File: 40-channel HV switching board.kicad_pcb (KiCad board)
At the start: 2 copper layers, 83.8 x 121.9 mm, 211 parts, among them IC1 ATMEG328PU, J1 CONN_01X04, J2 CONN_01X10, J3 BNC, J4 BNC, J5 CONN_01X40, P1 CONN_01X06, P2 CONN_01X06, SW1 Switch_DPST, U1 74HC595A, U2 74HC595A, U3 74HC595A, U4 74HC595A, U5 74HC595A, U6 7400, X1 16MHz

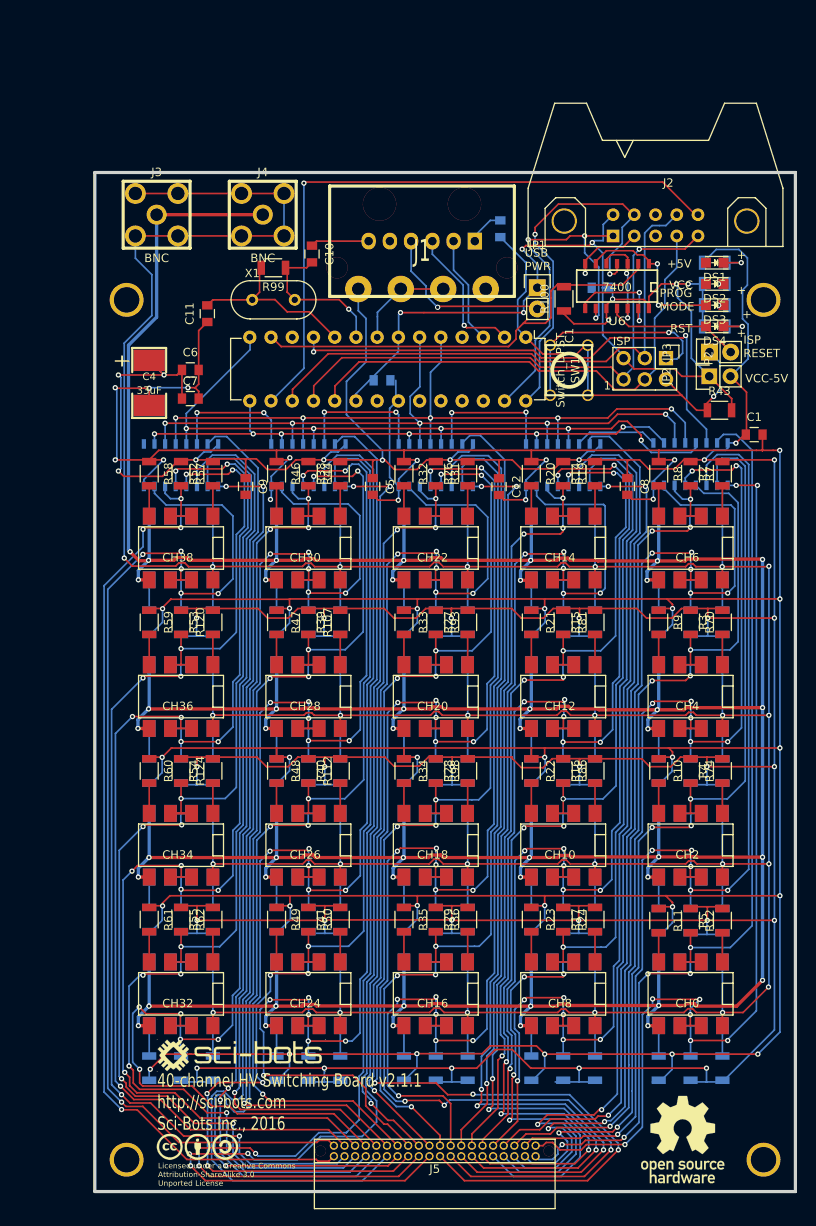
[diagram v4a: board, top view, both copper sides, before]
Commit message: Use edge connector, 3.3V logic, smaller board, etc.
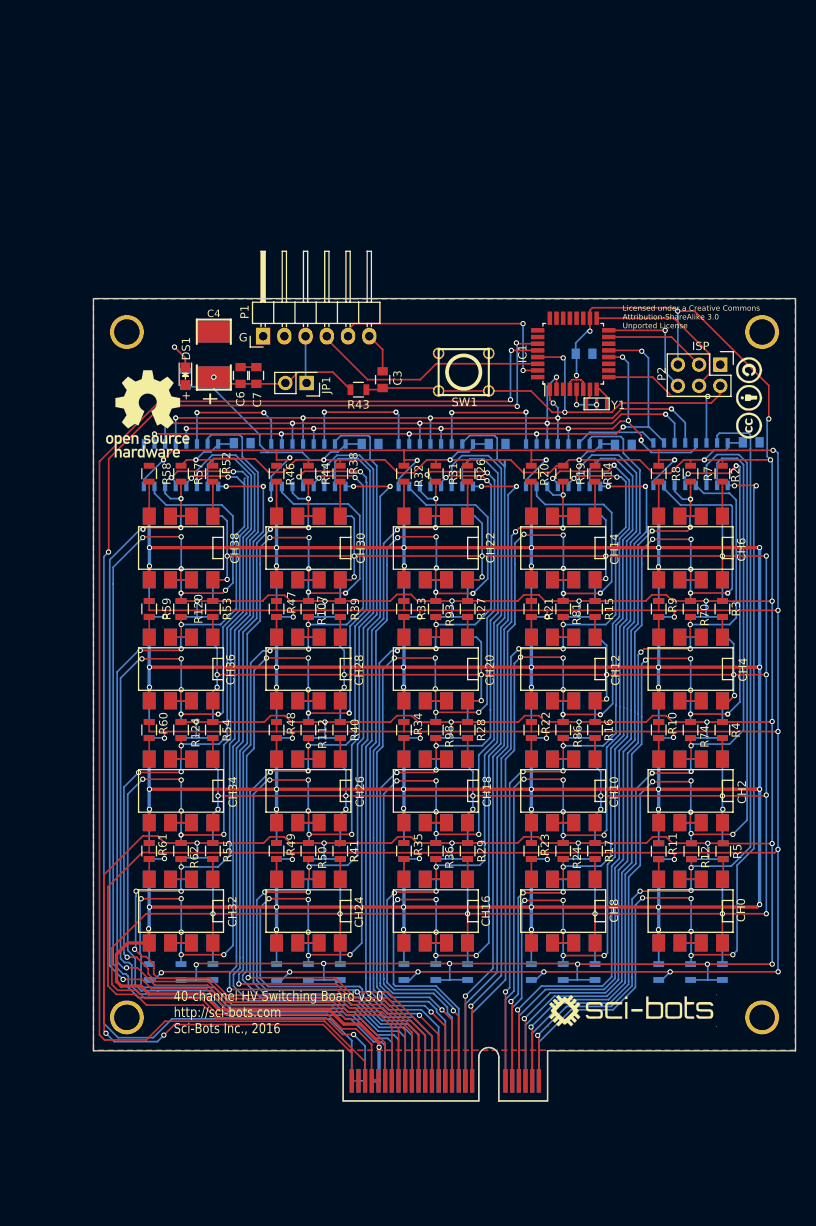
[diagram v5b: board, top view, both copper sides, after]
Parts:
- removed C10, C11: 22pF, Capacitors_SMD:C_0805
- removed C14: 0.1uF, Capacitors_SMD:C_0805
- removed DS2: VCC, LEDs:LED_0805
- removed DS3: PROG_MODE, LEDs:LED_0805
- removed DS4: RST, LEDs:LED_0805
- removed J1: CONN_01X04, footprints:Molex_15-24-4441
- removed J2: CONN_01X10, Connect:HE10-10C
- removed J3, J4: BNC, footprints:JACK_SMA
- removed J5: CONN_01X40, footprints:TFML-120-01-XXX-D-RA
- removed JP2: JUMPER, Pin_Headers:Pin_Header_Straight_1x02
- removed JP3: ISP RESET, Pin_Headers:Pin_Header_Straight_1x02
- removed R100, R125, R126, R127: 1k, Resistors_SMD:R_1206
- removed R99: 1Meg, Resistors_SMD:R_1206
- removed U6: 7400, footprints:SO14E
- removed X1: 16MHz, Crystals:HC-49V
- added P3: CONN_02X25, WheelerLab:HSEC8-125-XX-X-RA-MATE, F.Cu at (72.8, 132.8)
- added Y1: RESONATOR, WheelerLab:CSTCE_G15C, F.Cu at (85.7, 53.2)
- C1, C12, C5, C8, C9: moved to B.Cu
- C2, C4: footprint footprints:SM2917 -> WheelerLab:SM2917
- C3, P1: moved to F.Cu
- DS1: value +5V -> +3.3V_PWR
- G***: footprint footprints:OSHW_logo_10mm -> WheelerLab:OSHW_logo_10mm
- G***: footprint footprints:CC_S_A_logo_10mm -> WheelerLab:CC_S_A_logo_10mm
- IC1: value ATMEG328PU -> ATMEGA328P-A; footprint Housings_DIP:DIP-28_W7.62mm -> Housings_QFP:TQFP-32_7x7mm_Pitch0.8mm
- JP1: footprint Pin_Headers:Pin_Header_Straight_1x02 -> Pin_Headers:Pin_Header_Straight_2x01
- R1, R101, R106, R107, R112, R114, R118, R12, R120, R124, R13, R18, R19, R24, R25, R30, R31, R36, R37, R42, R43, R44, R45, R50, R51, R56, R57, R6, R62, R64, R68, R7, R70, R74, R75, R80, R81, R86, R87, R92, R93, R98: footprint Resistors_SMD:R_1206 -> Resistors_SMD:R_0805
- R10, R102, R103, R104, R105, R108, R109, R11, R110, R111, R113, R115, R116, R117, R119, R121, R122, R123, R14, R15, R16, R17, R2, R20, R21, R22, R23, R26, R27, R28, R29, R3, R32, R33, R34, R35, R38, R39, R4, R40, R41, R46, R47, R48, R49, R5, R52, R53, R54, R55, R58, R59, R60, R61, R63, R65, R66, R67, R69, R71, R72, R73, R76, R77, R78, R79, R8, R82, R83, R84, R85, R88, R89, R9, R90, R91, R94, R95, R96, R97: value 375 -> 300; footprint Resistors_SMD:R_1206 -> Resistors_SMD:R_0805
- SW1: footprint footprints:SW_PUSH_6mm -> WheelerLab:SW_PUSH_6mm
- U1, U2, U3, U4, U5: footprint footprints:SO16E -> WheelerLab:SO16E
- moved G*** 111.2 mm to (103.9, 52.5), turned to 90 degrees
- moved G*** 107.9 mm to (32.0, 54.4)
- moved R45 64.8 mm to (36.5, 50.2), turned to 90 degrees
- moved DS1 64.8 mm to (36.5, 49.9), turned to 270 degrees
- moved G*** 47.1 mm to (90.0, 125.8)
- moved R43 43.3 mm to (57.2, 51.5), turned to 180 degrees
- moved JP1 29.9 mm to (51.0, 50.7), turned to 180 degrees
- moved P1 27.8 mm to (45.8, 45.1)
- moved C13 24.4 mm to (84.2, 47.2)
- moved C3 22.9 mm to (60.1, 50.3)
- moved 1PIN 17.0 mm to (105.5, 126.6)
- moved 1PIN 17.0 mm to (29.5, 126.6)
- moved SW1 12.6 mm to (69.8, 49.4), turned to 180 degrees
- moved R101 11.5 mm to (51.2, 121.2)
- moved R102 11.5 mm to (55.0, 121.2)
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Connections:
- C1 pad 1: +5V -> +3.3V
- C12 pad 1: +5V -> +3.3V
- C13 pad 2: VCC -> +3.3V
- C2 pad 1: +5V -> +3.3V
- C4 pad 1: +5V -> +3.3V
- C5 pad 1: +5V -> +3.3V
- C6 pad 1: +5V -> +3.3V
- C7 pad 1: +5V -> +3.3V
- C8 pad 1: +5V -> +3.3V
- C9 pad 1: +5V -> +3.3V
- IC1 pad 1: RST -> D3/S_SS
- IC1 pad 11: D5/S_MOSI -> D7
- IC1 pad 12: Net-(IC1-Pad12) -> D8/OE
- IC1 pad 13: D7 -> D9/SRCLR
- IC1 pad 14: D8/OE -> D10/SS
- IC1 pad 15: D9/SRCLR -> D11/MOSI
- IC1 pad 16: D10/SS -> D12/MISO
- IC1 pad 17: D11/MOSI -> D13/SCK
- IC1 pad 18: D12/MISO -> +3.3V
- IC1 pad 19: D13/SCK -> Net-(IC1-Pad19)
- IC1 pad 2: TX -> D4/S_SCK
- IC1 pad 20: VCC -> Net-(IC1-Pad20)
- IC1 pad 21: Net-(IC1-Pad21) -> GND
- IC1 pad 22: GND -> Net-(IC1-Pad22)
- IC1 pad 3: RX -> GND
- IC1 pad 4: Net-(IC1-Pad4) -> +3.3V
- IC1 pad 5: D3/S_SS -> GND
- IC1 pad 6: D4/S_SCK -> +3.3V
- IC1 pad 7: VCC -> Net-(IC1-Pad7)
- IC1 pad 8: GND -> Net-(IC1-Pad8)
- IC1 pad 9: Net-(C10-Pad2) -> D5/S_MOSI
- JP1 pad 1: VCC -> +3.3V_USB
- JP1 pad 2: +5V_USB -> +3.3V
- P1 pad 1: Net-(C3-Pad1) -> GND
- P1 pad 2: RX -> Net-(P1-Pad2)
- P1 pad 3: TX -> +3.3V_USB
- P1 pad 4: +5V_USB -> TX
- P1 pad 5: Net-(P1-Pad5) -> RX
- P1 pad 6: GND -> Net-(C3-Pad1)
- P2 pad 5: VCC -> +3.3V
- R1 pad 1: +5V -> +3.3V
- R101 pad 1: +5V -> +3.3V
- R102 pad 2: +5V -> +3.3V
- R103 pad 2: +5V -> +3.3V
- R104 pad 2: +5V -> +3.3V
- R105 pad 2: +5V -> +3.3V
- R106 pad 1: +5V -> +3.3V
- R107 pad 1: +5V -> +3.3V
- R112 pad 1: +5V -> +3.3V
- R113 pad 2: +5V -> +3.3V
- R114 pad 1: +5V -> +3.3V
- R115 pad 2: +5V -> +3.3V
- R116 pad 2: +5V -> +3.3V
- R117 pad 2: +5V -> +3.3V
- R118 pad 1: +5V -> +3.3V
- R12 pad 1: +5V -> +3.3V
- R120 pad 1: +5V -> +3.3V
- R124 pad 1: +5V -> +3.3V
- R13 pad 1: +5V -> +3.3V
- R14 pad 2: +5V -> +3.3V
- R15 pad 2: +5V -> +3.3V
- R16 pad 2: +5V -> +3.3V
- R17 pad 2: +5V -> +3.3V
- R18 pad 1: +5V -> +3.3V
- R19 pad 1: +5V -> +3.3V
- R2 pad 2: +5V -> +3.3V
- R24 pad 1: +5V -> +3.3V
- R25 pad 1: +5V -> +3.3V
- R26 pad 2: +5V -> +3.3V
- R27 pad 2: +5V -> +3.3V
- R28 pad 2: +5V -> +3.3V
- R29 pad 2: +5V -> +3.3V
- R3 pad 2: +5V -> +3.3V
- R30 pad 1: +5V -> +3.3V
- R31 pad 1: +5V -> +3.3V
- R36 pad 1: +5V -> +3.3V
- R37 pad 1: +5V -> +3.3V
- R38 pad 2: +5V -> +3.3V
- R39 pad 2: +5V -> +3.3V
- R4 pad 2: +5V -> +3.3V
- R40 pad 2: +5V -> +3.3V
- R41 pad 2: +5V -> +3.3V
- R42 pad 1: +5V -> +3.3V
- R43 pad 2: VCC -> +3.3V
- R44 pad 1: +5V -> +3.3V
- R45 pad 1: +5V -> +3.3V
- R5 pad 2: +5V -> +3.3V
- R50 pad 1: +5V -> +3.3V
- R51 pad 1: +5V -> +3.3V
- R52 pad 2: +5V -> +3.3V
- R53 pad 2: +5V -> +3.3V
- R54 pad 2: +5V -> +3.3V
- R55 pad 2: +5V -> +3.3V
- R56 pad 1: +5V -> +3.3V
- R57 pad 1: +5V -> +3.3V
- R6 pad 1: +5V -> +3.3V
- R62 pad 1: +5V -> +3.3V
- R63 pad 2: +5V -> +3.3V
- R64 pad 1: +5V -> +3.3V
- R65 pad 2: +5V -> +3.3V
- R66 pad 2: +5V -> +3.3V
- R67 pad 2: +5V -> +3.3V
- R68 pad 1: +5V -> +3.3V
- R7 pad 1: +5V -> +3.3V
- R70 pad 1: +5V -> +3.3V
- R74 pad 1: +5V -> +3.3V
- R75 pad 1: +5V -> +3.3V
- R76 pad 2: +5V -> +3.3V
- R77 pad 2: +5V -> +3.3V
- R78 pad 2: +5V -> +3.3V
- R79 pad 2: +5V -> +3.3V
- R80 pad 1: +5V -> +3.3V
- R81 pad 1: +5V -> +3.3V
- R86 pad 1: +5V -> +3.3V
- R87 pad 1: +5V -> +3.3V
- R88 pad 2: +5V -> +3.3V
- R89 pad 2: +5V -> +3.3V
- R90 pad 2: +5V -> +3.3V
- R91 pad 2: +5V -> +3.3V
- R92 pad 1: +5V -> +3.3V
- R93 pad 1: +5V -> +3.3V
- R98 pad 1: +5V -> +3.3V
- U1 pad 16: +5V -> +3.3V
- U2 pad 16: +5V -> +3.3V
- U3 pad 16: +5V -> +3.3V
- U4 pad 16: +5V -> +3.3V
- U5 pad 16: +5V -> +3.3V
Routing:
- net +3.3V: track 0.00 -> 736.9 mm, vias 0 -> 37
- net +5V: track 714.0 -> 0.00 mm, vias 34 -> 0
- net VCC: track 125.3 -> 0.00 mm, vias 8 -> 0
- net GND: track 723.0 -> 598.9 mm, vias 40 -> 34
- net A4/SDA: track 44.8 -> 166.8 mm
- net A5/SCL: track 46.8 -> 167.2 mm
- net D10/SS: track 76.5 -> 0.00 mm, vias 1 -> 0
- net HV: track 597.1 -> 536.8 mm
- net D11/MOSI: track 66.5 -> 12.2 mm
- net HVOUT21: track 120.4 -> 67.7 mm, vias 5 -> 3
- net D7: track 52.1 -> 0.00 mm
- net D12/MISO: track 65.4 -> 14.0 mm
- net HVOUT23: track 132.6 -> 81.9 mm, vias 5 -> 3
- net HVOUT19: track 97.5 -> 52.6 mm, vias 5 -> 3
- net D5/S_MOSI: track 61.7 -> 18.4 mm, vias 2 -> 1
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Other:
- board size 83.8 x 121.9 mm -> 84 x 96 mm
- net class HV removed
- net class PWR added: clearance 0.2032, trace_width 0.39878, via_dia 0.635, via_drill 0.381
- board text added: "40-channel HV Switching Board v3.0 http://sci-bots.com Sci-Bots Inc., 2016"
- board text removed: "+5V"
- board text removed: "1"
- board text removed: "40-channel HV Switching Board v2.1.1 http://sci-bots.com Sci-Bots Inc., 2016"
- board text removed: "ISP RESET"
- board text removed: "PROG MODE"
- board text removed: "RST"
- board text removed: "USB PWR"
- board text removed: "VCC"
- board text removed: "VCC-5V"

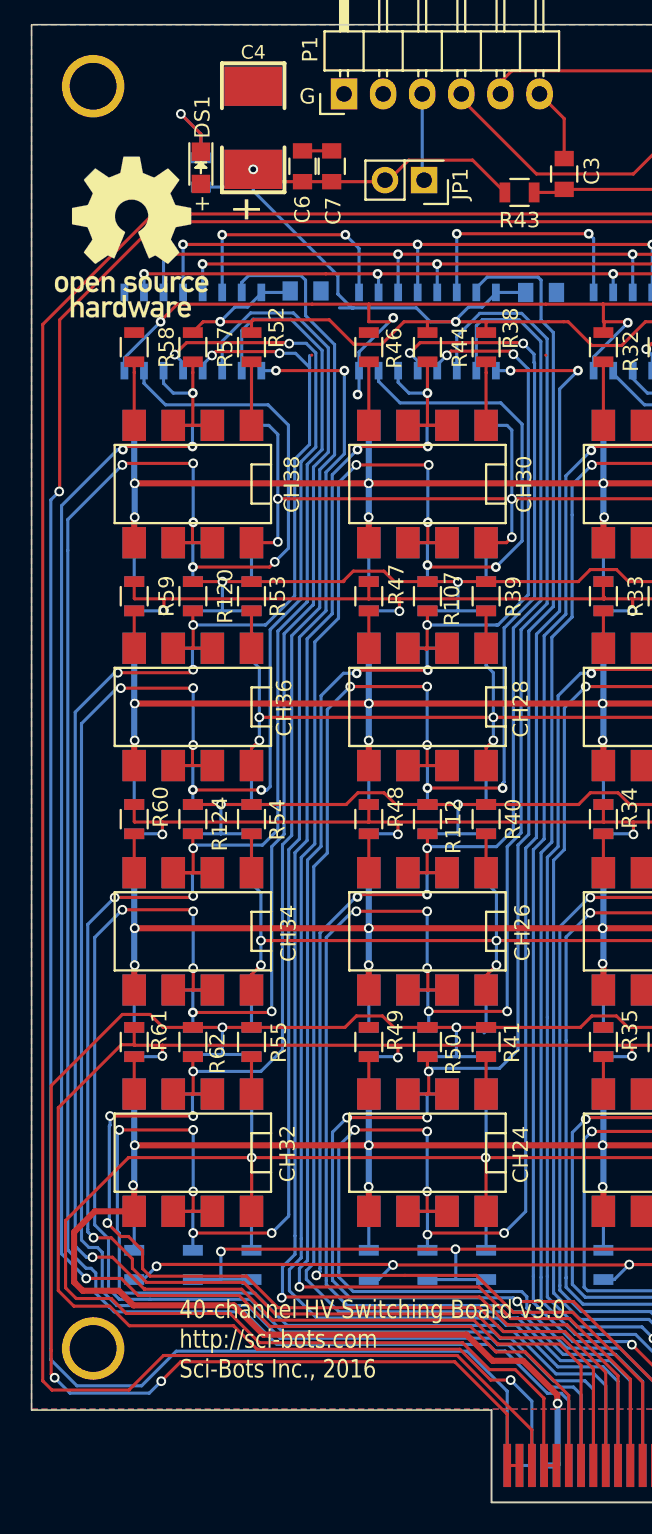
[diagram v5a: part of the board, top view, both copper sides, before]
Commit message: Breakout reset pin to edge connector
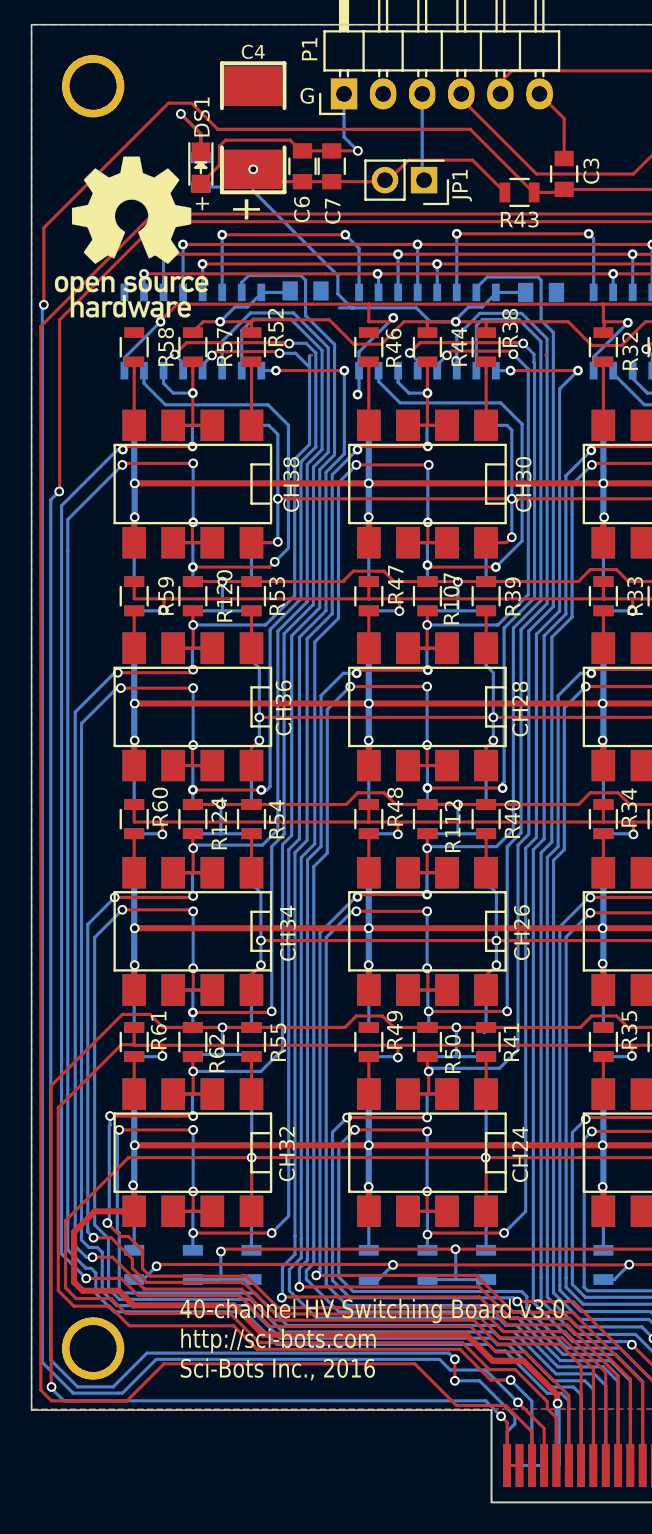
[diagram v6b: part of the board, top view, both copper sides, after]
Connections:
- P3 pad 43: HV -> GND
- P3 pad 44: HVGND -> RST
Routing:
- net RST: track 55.2 -> 205.2 mm, vias 2 -> 4
- net GND: track 598.9 -> 614.3 mm, vias 34 -> 35
- net +3.3V: track 736.9 -> 735.5 mm
- net HV: track 536.8 -> 536.0 mm
- net A5/SCL: track 167.2 -> 167.8 mm
- net A4/SDA: track 166.8 -> 167.3 mm, vias 3 -> 5
- net HVGND: track 536.5 -> 536.0 mm

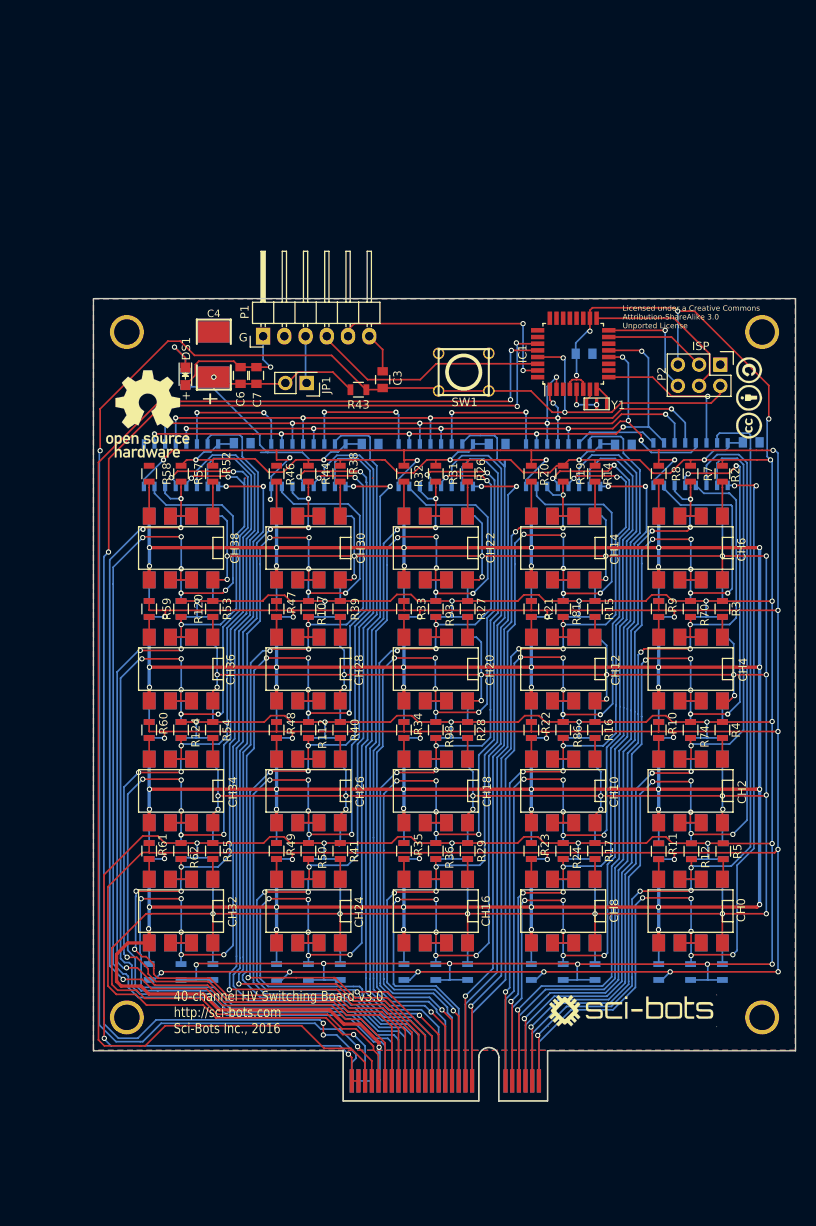
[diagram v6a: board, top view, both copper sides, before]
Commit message: Add SPI flash memory, move edge connector to side
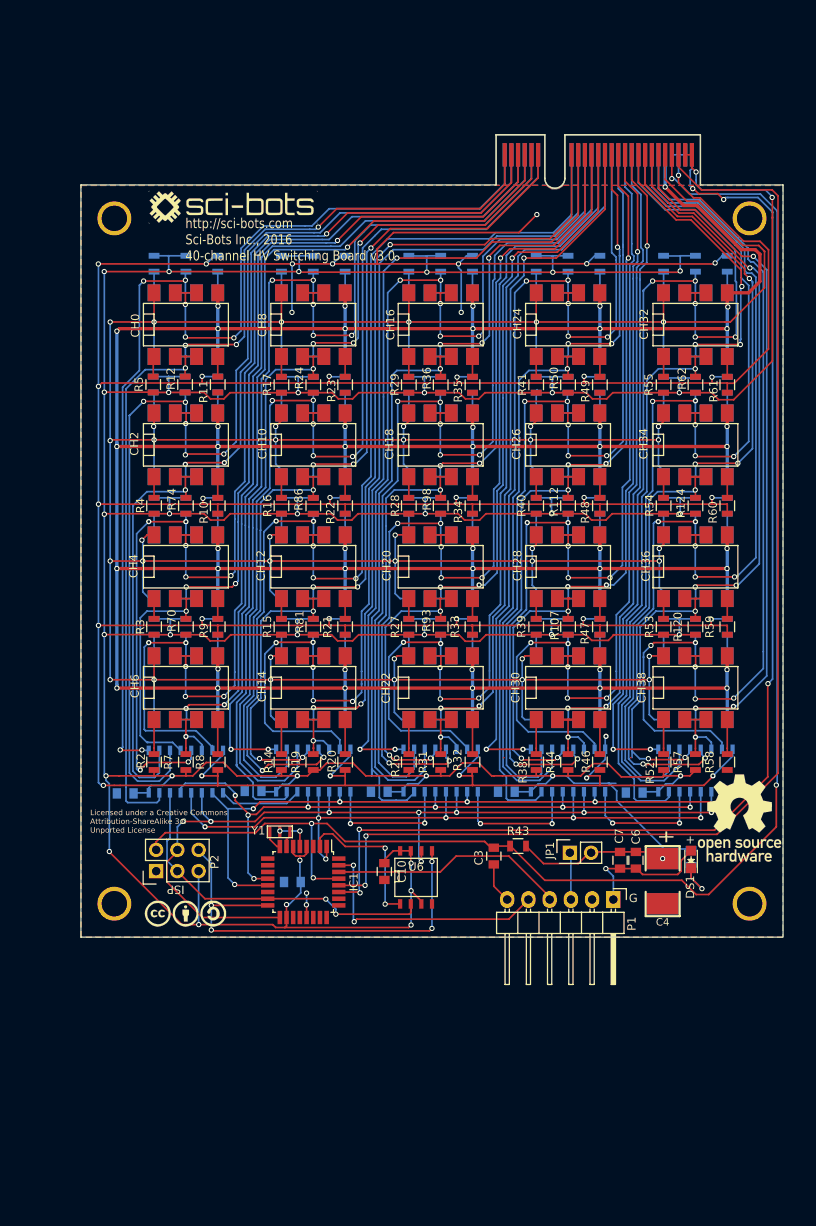
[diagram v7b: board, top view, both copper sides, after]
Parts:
- removed SW1: Switch_DPST, WheelerLab:SW_PUSH_6mm
- added C10: 0.1uF, Capacitors_SMD:C_0805, F.Cu at (60.3, 109.2)
- added U6: W25Q64FV, SMD_Packages:SOIC-8-N, F.Cu at (64.1, 109.8)
- moved 1PIN 123.1 mm to (28.0, 31.0), turned to 90 degrees
- moved 1PIN 121.2 mm to (104.0, 31.0), turned to 90 degrees
- moved R119 109.4 mm to (101.3, 36.4), turned to 270 degrees
- moved R63 108.7 mm to (32.8, 36.4), turned to 90 degrees
- moved P3 108.3 mm to (80.7, 24.8), turned to 0 degrees
- moved G*** 107.4 mm to (42.2, 29.6)
- moved R114 104.7 mm to (97.5, 36.4), turned to 270 degrees
- moved R64 104.1 mm to (36.6, 36.4), turned to 270 degrees
- moved 1PIN 103.4 mm to (28.0, 113.0), turned to 90 degrees
- moved 1PIN 101.1 mm to (104.0, 113.0), turned to 90 degrees
- moved R113 100.4 mm to (93.7, 36.4), turned to 90 degrees
- moved R69 99.8 mm to (40.4, 36.4), turned to 270 degrees
- moved CH32 93.3 mm to (97.5, 43.7), turned to 0 degrees
- moved CH33 93.3 mm to (97.5, 43.7), turned to 0 degrees
- moved R108 93.2 mm to (86.1, 36.4), turned to 270 degrees
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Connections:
- net D3/S_SS renamed D3/595SS
- IC1 pad 2: D4/S_SCK -> D4/W25SS
- IC1 pad 9: D5/S_MOSI -> Net-(IC1-Pad9)
- U1 pad 11: D4/S_SCK -> D13/SCK
- U1 pad 14: D5/S_MOSI -> D11/MOSI
- U2 pad 11: D4/S_SCK -> D13/SCK
- U3 pad 11: D4/S_SCK -> D13/SCK
- U4 pad 11: D4/S_SCK -> D13/SCK
- U5 pad 11: D4/S_SCK -> D13/SCK
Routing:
- net D13/SCK: track 19.6 -> 108.2 mm, vias 0 -> 8
- net D4/S_SCK: track 81.7 -> 0.00 mm, vias 6 -> 0
- net D12/MISO: track 14.0 -> 53.0 mm, vias 1 -> 4
- net D11/MOSI: track 12.2 -> 41.6 mm, vias 0 -> 2
- net A4/SDA: track 167.3 -> 144.8 mm
- net A5/SCL: track 167.8 -> 145.4 mm
- net HVOUT37: track 90.1 -> 68.4 mm
- net HVOUT35: track 74.8 -> 53.2 mm
- net RST: track 205.2 -> 183.6 mm
- net HVOUT33: track 59.7 -> 38.5 mm
- net HVOUT32: track 62.5 -> 41.5 mm
- net HVOUT34: track 77.2 -> 56.4 mm
- net HVOUT36: track 92.0 -> 71.6 mm
- net HV: track 536.0 -> 515.5 mm
- net HVGND: track 536.0 -> 515.7 mm
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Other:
- outline, holes or cut-outs redrawn
- board text added: "http://sci-bots.com Sci-Bots Inc., 2016 40-channel HV Switching Board v3.0"
- board text removed: "40-channel HV Switching Board v3.0 http://sci-bots.com Sci-Bots Inc., 2016"
